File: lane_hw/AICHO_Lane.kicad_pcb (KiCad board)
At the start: 2 copper layers, 65 parts, among them J1 JST PH, J2 RJ45, J41 JST PH, J42 JST PH, J43 JST PH, J9 Conn_01x04, Q41 AO3400A, Q42 AO3400A, Q43 AO3400A, U1 TPS54302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

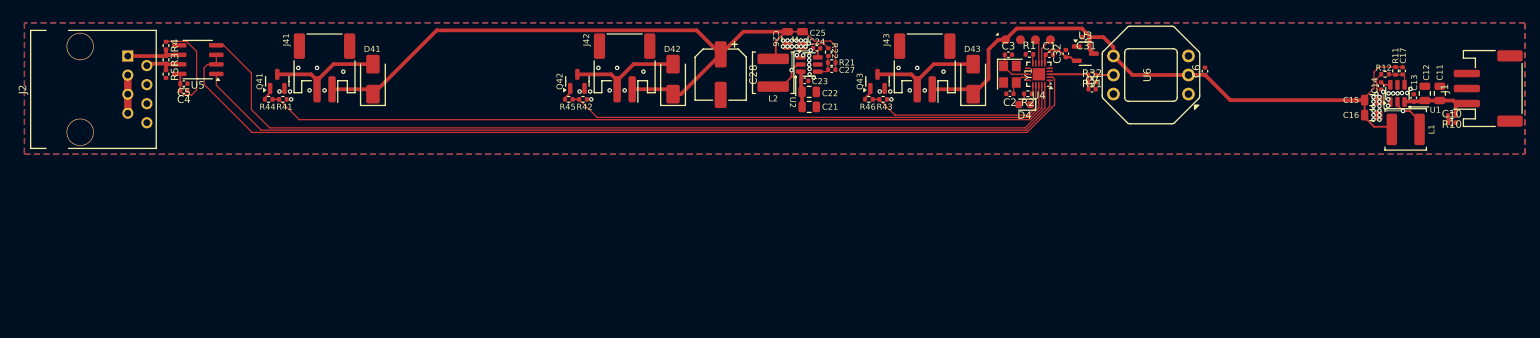
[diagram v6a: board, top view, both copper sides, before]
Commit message: lane_hw: Revise board dimensions and layout
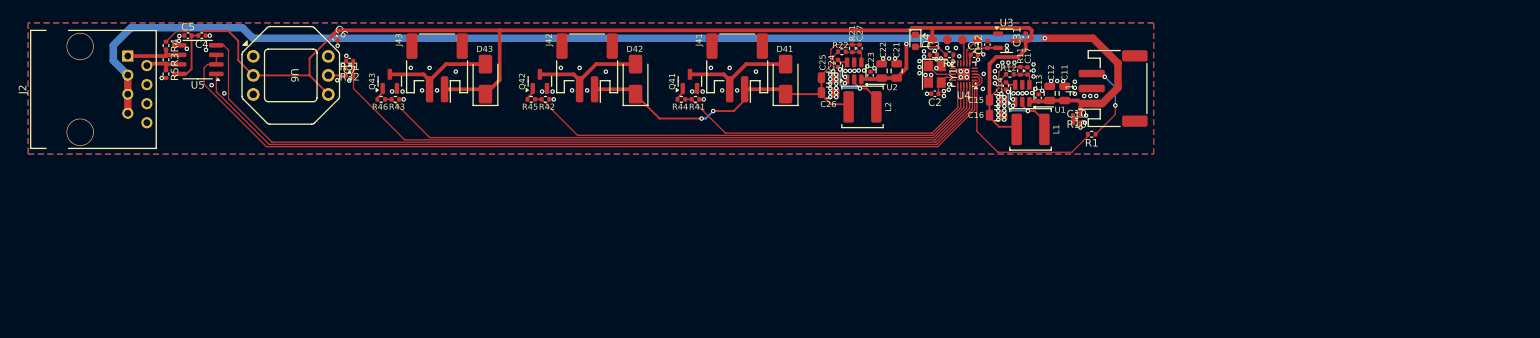
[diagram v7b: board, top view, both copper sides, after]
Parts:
- removed C28: 220u 25V, Capacitor_SMD:CP_Elec_6.3x7.7
- moved C6 116.0 mm to (91.4, 42.0), turned to -45 degrees
- moved U6 114.7 mm to (85.5, 47.0), turned to -90 degrees
- moved C7 99.0 mm to (93.3, 45.1), turned to 180 degrees
- moved R32 99.0 mm to (93.3, 46.0), turned to 180 degrees
- moved R31 99.0 mm to (93.3, 47.0), turned to 0 degrees
- moved R46 65.0 mm to (97.5, 50.2)
- moved J43 65.0 mm to (105.0, 46.0)
- moved D43 65.0 mm to (111.5, 47.5)
- moved Q43 65.0 mm to (98.7, 47.8)
- moved R43 65.0 mm to (99.5, 50.2)
- moved R44 55.0 mm to (137.6, 50.2)
- moved J41 55.0 mm to (145.0, 46.0)
- moved D41 55.0 mm to (151.4, 47.5)
- moved Q41 55.0 mm to (138.7, 47.8)
- moved R41 55.0 mm to (139.4, 50.2)
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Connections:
- U4 pad 10: /UART1_TX -> unconnected-(U4-PB6-Pad10)
- U4 pad 11: unconnected-(U4-PB7-Pad11) -> /ACT_LED
- U4 pad 16: /ACT_LED -> /PUMP_1
- U4 pad 17: /PUMP_3 -> /PUMP_2
- U4 pad 18: /PUMP_2 -> /PUMP_3
- U4 pad 19: /PUMP_1 -> /PRESSURE_SENSOR
- U4 pad 3: /PRESSURE_SENSOR -> /UART1_TX
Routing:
- net +24V: track 21.3 -> 175.6 mm, vias 0 -> 2
- net /PRESSURE_SENSOR: track 7.09 -> 93.1 mm
- net +5V: track 100.2 -> 180.7 mm
- net /PUMP_1: track 107.4 -> 42.6 mm
- net /PUMP_3: track 26.0 -> 83.9 mm
- net +12V: track 95.8 -> 49.2 mm, vias 0 -> 2
- net /UART1_TX: track 1.22 -> 25.8 mm
- net Net-(J1-Pin_3): track 0.00 -> 11.3 mm, vias 0 -> 2
- net /DE: track 127.0 -> 118.8 mm
- net /UART2_RX: track 119.9 -> 111.9 mm
- net /UART2_TX: track 122.0 -> 114.5 mm
- net /PUMP_2: track 66.7 -> 63.3 mm
- net Net-(D4-A): track 1.75 -> 4.48 mm
- net +3V3: track 6.16 -> 5.22 mm
- net /ACT_LED: track 1.21 -> 1.82 mm
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
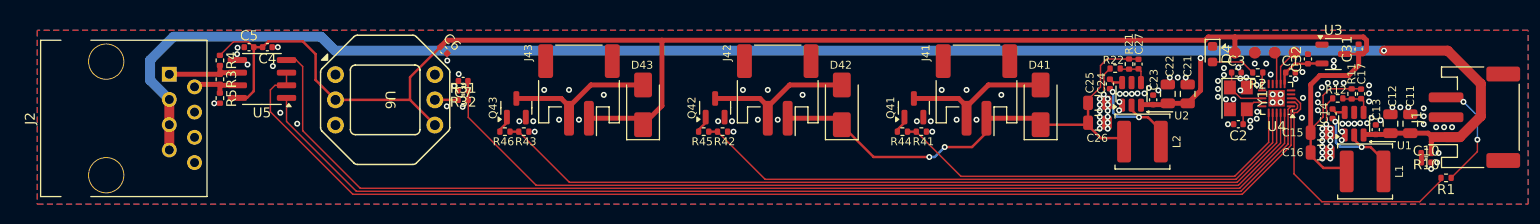
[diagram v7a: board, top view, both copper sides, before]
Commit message: lane_hw: Adjust layout & finish routing
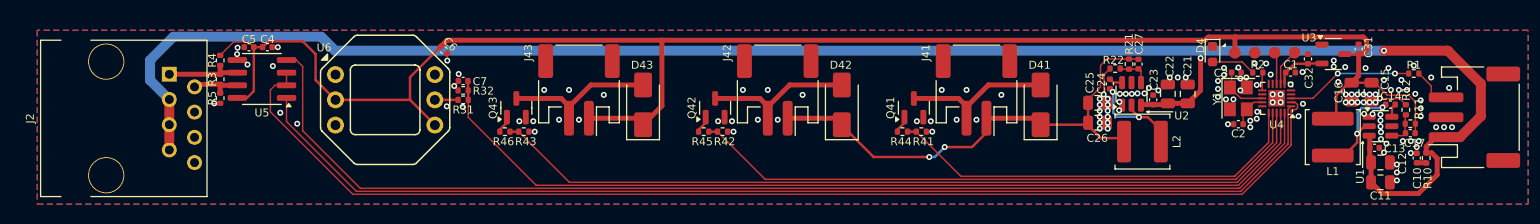
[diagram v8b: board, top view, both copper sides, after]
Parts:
- moved R1 11.0 mm to (189.0, 44.4)
- moved R12 6.95 mm to (188.2, 48.0), turned to 90 degrees
- moved C16 6.85 mm to (182.8, 46.2), turned to -90 degrees
- moved R11 6.62 mm to (188.7, 49.4), turned to 180 degrees
- moved C11 6.62 mm to (185.7, 55.3), turned to 0 degrees
- moved C15 6.59 mm to (184.8, 46.2), turned to -90 degrees
- moved C17 6.33 mm to (188.7, 50.4), turned to 180 degrees
- moved C14 5.90 mm to (186.7, 47.5), turned to 180 degrees
- moved L1 4.74 mm to (180.8, 50.8), turned to 90 degrees
- moved C12 4.03 mm to (185.7, 53.3), turned to 0 degrees
- moved U1 2.66 mm to (185.7, 49.6), turned to 0 degrees
- moved C13 1.83 mm to (185.1, 51.8), turned to 0 degrees
- moved C10 1.05 mm to (189.3, 52.9), turned to 90 degrees
- moved R10 0.50 mm to (190.2, 52.9), turned to -90 degrees
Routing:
- net /UART1_TX: track 25.8 -> 12.9 mm, vias 0 -> 2
- net +24V: track 175.6 -> 184.3 mm
- net +5V: track 180.7 -> 172.2 mm
- net Net-(J1-Pin_3): track 11.3 -> 4.27 mm, vias 2 -> 0
- net GND: vias 136 -> 141
